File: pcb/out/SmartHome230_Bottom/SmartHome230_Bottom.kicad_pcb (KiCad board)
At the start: 2 copper layers, 130 x 115 mm, 58 parts, among them J1 B2B, J2 12V, J3 Przyciski A, J4 Przyciski B, J5 UART, J6 230V IN, J7 Wyj.1, J8 Wyj.2, K1 SRD-12V, K2 SRD-12V, Q1 BC547, Q2 BC547, SW1 EN, SW2 BOOT, U1 MP1584, U2 AMS1117-3.3, U3 ESP32-WROOM-32

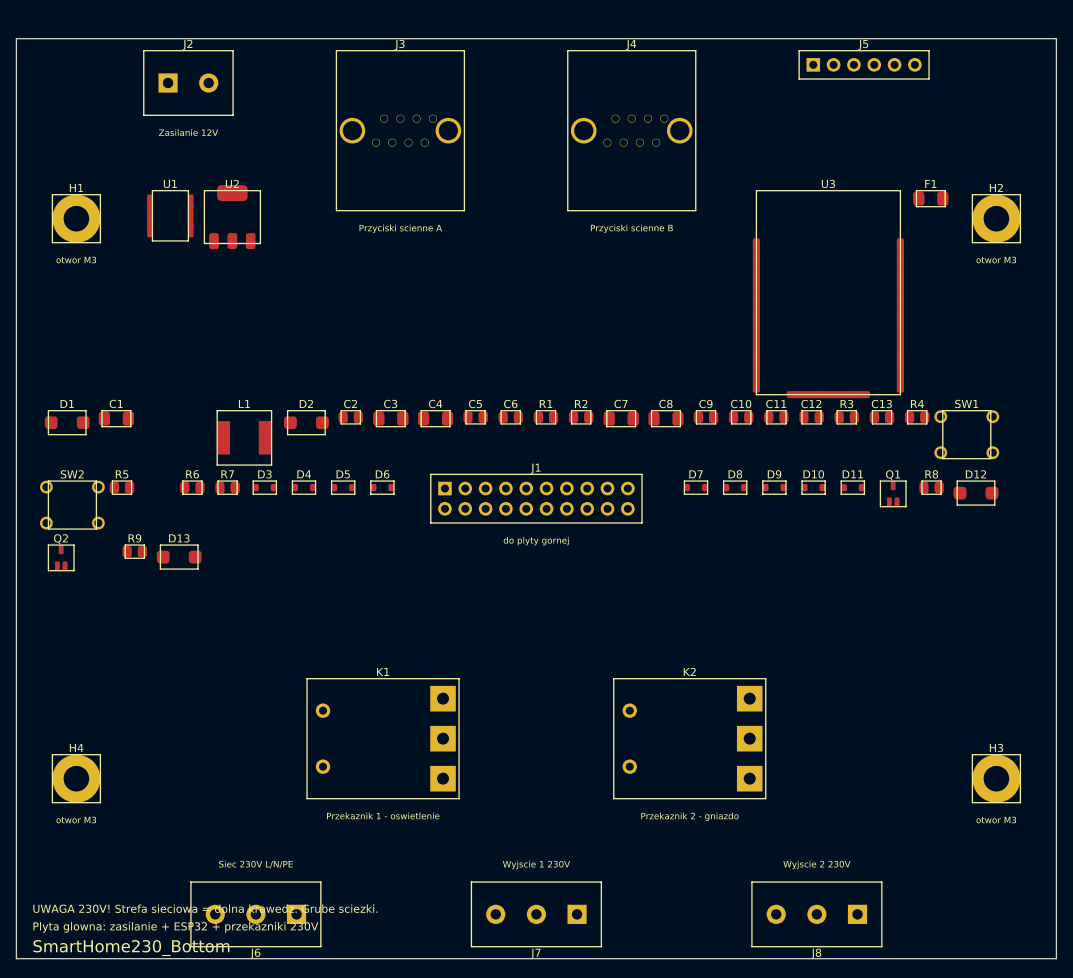
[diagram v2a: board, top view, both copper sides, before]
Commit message: HomeController PRO: sterownik domowy 32 wej / 16 wyj (2 plyty, 24V)
Nowe czesci: ESP32-C3 (modul kastelowany), TJA1051 (CAN), MOV (warystor),
MOSFET mocy DPAK (TO-252). Nowe bloki: wyjscie przekaznikowe 230V, wyjscie
MOSFET DC, bank wejsc RJ45 (TVS/wejscie), RS485, CAN, ESP32-C3, zlacze TFT.

Plyta DOLNA: 24V (bezpiecznik+dioda+MOV+buck5V+LDO3V3), ekspander wyjsc,
8x przekaznik 230V + 8x MOSFET DC, kazde wlasny zacisk; przekazniki we wnetrzu.
Plyta GORNA (wezsza): ESP32-C3 + 2x ekspander (32 wejscia), 8x RJ45, RS485+CAN,
TFT dotykowy. Otwory + B2B wspolne 1:1.

Layout: I/O na krawedzi dla OBU plyt (omija otwory narozne), zaciski 230V na
dolnej krawedzi, przekazniki we wnetrzu. Heurystyka zasilania rozpoznaje V24/Vxx;
regula diod tylko dla zlacz polowych (RJ45/zaciski). Niezawodnosc: TVS na kazdym
I/O, MOV, diody gasnace, pull-down bramek, grube sciezki 230V.

Oba PCB 0/0/0, zwalidowane kiutils (140 i 77 footprintow). Testy 12/12.

Co-Authored-By: Claude Opus 4.8 (1M context) <noreply@anthropic.com>
Claude-Session: https://claude.ai/code/session_01LNGxtK2Jv1rJLBLPTwFQ9C
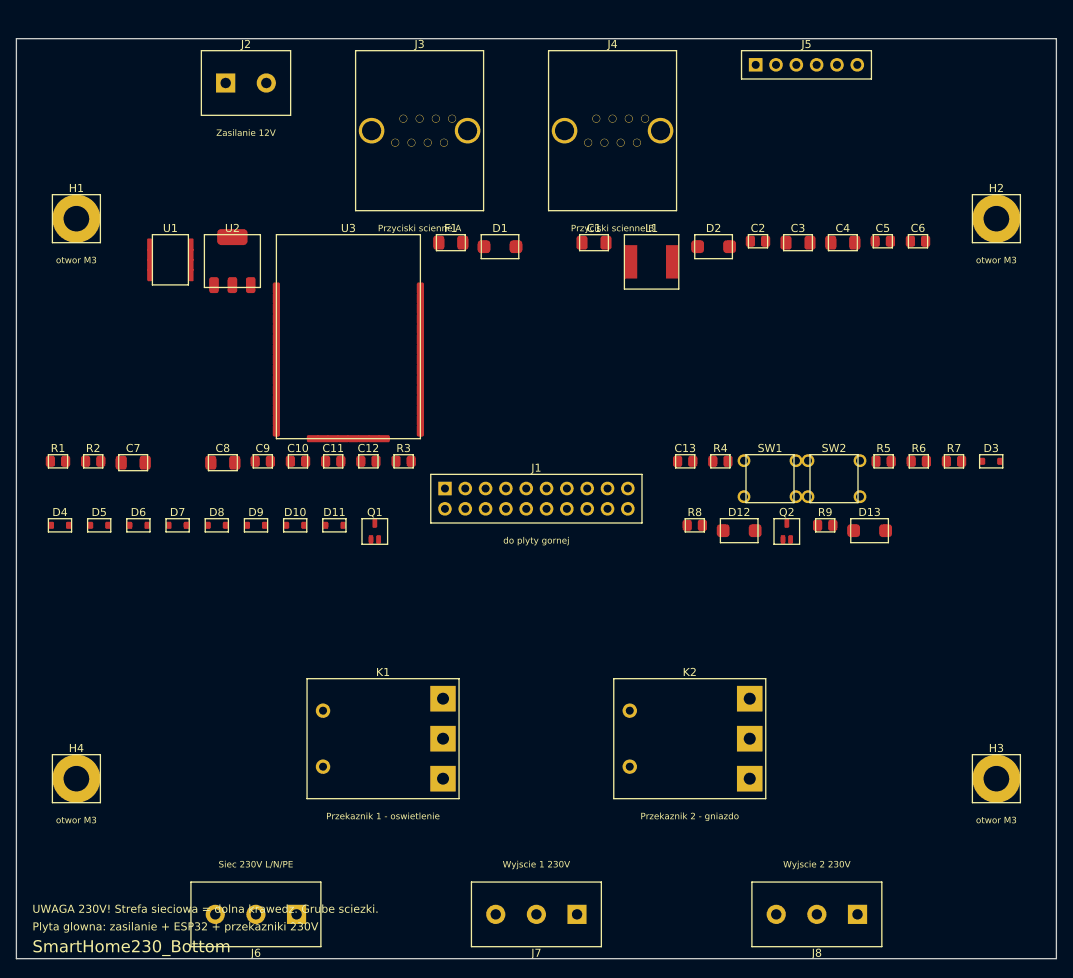
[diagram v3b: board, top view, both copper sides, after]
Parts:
- moved SW2 95.3 mm to (102.2, 55.0)
- moved R5 95.3 mm to (108.4, 52.8)
- moved R7 90.9 mm to (117.2, 52.8)
- moved D3 90.9 mm to (121.8, 52.8)
- moved R6 90.9 mm to (112.8, 52.8)
- moved Q2 90.8 mm to (96.3, 61.6)
- moved D13 86.4 mm to (106.7, 61.5)
- moved R9 86.4 mm to (101.1, 60.8)
- moved D10 65.0 mm to (34.9, 60.8)
- moved D7 65.0 mm to (20.1, 60.8)
- moved D11 65.0 mm to (39.8, 60.8)
- moved D8 65.0 mm to (25.1, 60.8)
- moved D9 65.0 mm to (29.9, 60.8)
- moved Q1 65.0 mm to (44.8, 61.6)
- moved C1 63.6 mm to (72.2, 25.5)
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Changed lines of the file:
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@@
     "pcbforge:ScrewTerminal_1x02_P5.08mm"
     (layer "F.Cu")
-    (at 21.5 5.54)
+    (at 28.7 5.54)
     (descr "Listwa zaciskowa 2x5.08mm")
     (attr through_hole)
@@
     "pcbforge:RJ45_8P8C"
     (layer "F.Cu")
-    (at 48 11.5)
+    (at 50.4 11.5)
     (descr "Gniazdo RJ45 8P8C THT")
     (attr through_hole)
@@
     "pcbforge:RJ45_8P8C"
     (layer "F.Cu")
-    (at 76.92 11.5)
+    (at 74.52 11.5)
     (descr "Gniazdo RJ45 8P8C THT")
     (attr through_hole)
@@
     "pcbforge:F_1206"
     (layer "F.Cu")
-    (at 114.3 20)
+    (at 54.3 25.5)
     (descr "F chip 1206")
     (attr smd)
@@
     "pcbforge:D_SMA"
     (layer "F.Cu")
-    (at 6.35 48)
+    (at 60.45 26)
     (descr "D_SMA")
     (attr smd)
@@
     "pcbforge:CP_1206"
     (layer "F.Cu")
-    (at 12.5 47.5)
+    (at 72.2 25.5)
     (descr "CP chip 1206")
     (attr smd)
@@
     "pcbforge:SOIC-8"
     (layer "F.Cu")
-    (at 19.25 22.14)
+    (at 19.25 27.64)
     (descr "SOIC-8 (1.27mm)")
     (attr smd)
@@
     "pcbforge:L_6x6"
     (layer "F.Cu")
-    (at 28.5 49.9)
+    (at 79.4 27.9)
     (descr "Cewka mocy 6x6mm")
     (attr smd)
@@
     "pcbforge:D_SMA"
     (layer "F.Cu")
-    (at 36.25 48)
+    (at 87.15 26)
     (descr "D_SMA")
     (attr smd)
@@
     "pcbforge:C_0805"
     (layer "F.Cu")
-    (at 41.8 47.33)
+    (at 92.7 25.32)
     (descr "C chip 0805")
     (attr smd)
@@
     "pcbforge:CP_1206"
     (layer "F.Cu")
-    (at 46.8 47.5)
+    (at 97.7 25.5)
     (descr "CP chip 1206")
     (attr smd)
@@
     "pcbforge:CP_1206"
     (layer "F.Cu")
-    (at 52.4 47.5)
+    (at 103.3 25.5)
     (descr "CP chip 1206")
     (attr smd)
@@
     "pcbforge:C_0805"
     (layer "F.Cu")
-    (at 57.4 47.33)
+    (at 108.3 25.32)
     (descr "C chip 0805")
     (attr smd)
@@
     "pcbforge:C_0805"
     (layer "F.Cu")
-    (at 61.8 47.33)
+    (at 112.7 25.32)
     (descr "C chip 0805")
     (attr smd)
@@
     "pcbforge:R_0805"
     (layer "F.Cu")
-    (at 66.2 47.33)
+    (at 5.2 52.83)
     (descr "R chip 0805")
     (attr smd)
@@
     "pcbforge:R_0805"
     (layer "F.Cu")
-    (at 70.6 47.33)
+    (at 9.6 52.83)
     (descr "R chip 0805")
     (attr smd)
@@
     "pcbforge:SOT-223"
     (layer "F.Cu")
-    (at 27 22.3)
+    (at 27 27.8)
     (descr "SOT-223 (regulator LDO)")
     (attr smd)
@@
     "pcbforge:CP_1206"
     (layer "F.Cu")
-    (at 75.6 47.5)
+    (at 14.6 53)
     (descr "CP chip 1206")
     (attr smd)
@@
     "pcbforge:CP_1206"
     (layer "F.Cu")
-    (at 81.2 47.5)
+    (at 25.8 53)
     (descr "CP chip 1206")
     (attr smd)
@@
     "pcbforge:C_0805"
     (layer "F.Cu")
-    (at 86.2 47.33)
+    (at 30.8 52.83)
     (descr "C chip 0805")
     (attr smd)
@@
     "pcbforge:C_0805"
     (layer "F.Cu")
-    (at 90.6 47.33)
+    (at 35.2 52.83)
     (descr "C chip 0805")
     (attr smd)
@@
     "pcbforge:ESP32-WROOM-32"
     (layer "F.Cu")
-    (at 101.5 31.75)
+    (at 41.5 37.25)
     (descr "Modul ESP32-WROOM-32 (38 padow)")
     (attr smd)
@@
     "pcbforge:C_0805"
     (layer "F.Cu")
-    (at 95 47.33)
+    (at 39.6 52.83)
     (descr "C chip 0805")
     (attr smd)
@@
     "pcbforge:C_0805"
     (layer "F.Cu")
-    (at 99.4 47.33)
+    (at 44 52.83)
     (descr "C chip 0805")
     (attr smd)
@@
     "pcbforge:R_0805"
     (layer "F.Cu")
-    (at 103.8 47.33)
+    (at 48.4 52.83)
     (descr "R chip 0805")
     (attr smd)
@@
     "pcbforge:C_0805"
     (layer "F.Cu")
-    (at 108.2 47.33)
+    (at 83.6 52.83)
     (descr "C chip 0805")
     (attr smd)
@@
     "pcbforge:R_0805"
     (layer "F.Cu")
-    (at 112.6 47.33)
+    (at 88 52.83)
     (descr "R chip 0805")
     (attr smd)
@@
     "pcbforge:SW_Push_6mm"
     (layer "F.Cu")
-    (at 118.8 49.5)
+    (at 94.2 55)
     (descr "Tact switch 6mm")
     (attr through_hole)
@@
     "pcbforge:SW_Push_6mm"
     (layer "F.Cu")
-    (at 7 58.3)
+    (at 102.2 55)
     (descr "Tact switch 6mm")
     (attr through_hole)
@@
     "pcbforge:PinHeader_1x06_P2.54mm"
     (layer "F.Cu")
-    (at 105.96 3.27)
+    (at 98.76 3.27)
     (descr "Pin header 1x6")
     (attr through_hole)
@@
     "pcbforge:R_0805"
     (layer "F.Cu")
-    (at 13.2 56.12)
+    (at 108.4 52.83)
     (descr "R chip 0805")
     (attr smd)
@@
     "pcbforge:R_0805"
     (layer "F.Cu")
-    (at 22 56.12)
+    (at 112.8 52.83)
     (descr "R chip 0805")
     (attr smd)
@@
     "pcbforge:R_0805"
     (layer "F.Cu")
-    (at 26.4 56.12)
+    (at 117.2 52.83)
     (descr "R chip 0805")
     (attr smd)
@@
     "pcbforge:D_SOD-323"
     (layer "F.Cu")
-    (at 31.05 56.12)
+    (at 121.85 52.83)
     (descr "D_SOD-323")
     (attr smd)
@@
     "pcbforge:D_SOD-323"
     (layer "F.Cu")
-    (at 35.95 56.12)
+    (at 5.45 60.83)
     (descr "D_SOD-323")
     (attr smd)
@@
     "pcbforge:D_SOD-323"
     (layer "F.Cu")
-    (at 40.85 56.12)
+    (at 10.35 60.83)
     (descr "D_SOD-323")
     (attr smd)
@@
     "pcbforge:D_SOD-323"
     (layer "F.Cu")
-    (at 45.75 56.12)
+    (at 15.25 60.83)
     (descr "D_SOD-323")
     (attr smd)
@@
     "pcbforge:D_SOD-323"
     (layer "F.Cu")
-    (at 84.95 56.12)
+    (at 20.15 60.83)
     (descr "D_SOD-323")
     (attr smd)
@@
     "pcbforge:D_SOD-323"
     (layer "F.Cu")
-    (at 89.85 56.12)
+    (at 25.05 60.83)
     (descr "D_SOD-323")
     (attr smd)
@@
     "pcbforge:D_SOD-323"
     (layer "F.Cu")
-    (at 94.75 56.12)
+    (at 29.95 60.83)
     (descr "D_SOD-323")
     (attr smd)
@@
     "pcbforge:D_SOD-323"
     (layer "F.Cu")
-    (at 99.65 56.12)
+    (at 34.85 60.83)
     (descr "D_SOD-323")
     (attr smd)
@@
     "pcbforge:D_SOD-323"
     (layer "F.Cu")
-    (at 104.55 56.12)
+    (at 39.75 60.83)
     (descr "D_SOD-323")
     (attr smd)
@@
     "pcbforge:SOT-23-3"
     (layer "F.Cu")
-    (at 109.6 56.9)
+    (at 44.8 61.6)
     (descr "SOT-23-3")
     (attr smd)
@@
     "pcbforge:R_0805"
     (layer "F.Cu")
-    (at 114.4 56.12)
+    (at 84.8 60.83)
     (descr "R chip 0805")
     (attr smd)
@@
     "pcbforge:D_SMA"
     (layer "F.Cu")
-    (at 119.95 56.8)
+    (at 90.35 61.5)
     (descr "D_SMA")
     (attr smd)
@@
     "pcbforge:SOT-23-3"
     (layer "F.Cu")
-    (at 5.6 64.9)
+    (at 96.3 61.6)
     (descr "SOT-23-3")
     (attr smd)
@@
     "pcbforge:R_0805"
     (layer "F.Cu")
-    (at 14.8 64.12)
+    (at 101.1 60.83)
     (descr "R chip 0805")
     (attr smd)
@@
     "pcbforge:D_SMA"
     (layer "F.Cu")
-    (at 20.35 64.8)
+    (at 106.65 61.5)
     (descr "D_SMA")
     (attr smd)

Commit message: ESP32-S3 + przyciski TFT; kompaktowy layout (szerokosc z liczby zlacz, 2 rzedy)
- Przejscie ESP32-C3 -> ESP32-S3 (duzo GPIO): niezalezne RS485/CAN, dotyk z IRQ,
  4 przyciski nawigacji TFT (GORA/DOL/OK/WSTECZ). Nowa czesc ESP32-S3-WROOM-1.
- Layout: I/O wzdluz krawedzi w 2 rzedach (podwojne w pionie), szerokosc plytki
  wynika z LICZBY zlacz (zmienne szerokosci kolumn) - wejscia na gornej krawedzi,
  wyjscia (zaciski) na dolnej. auto_frame() dobiera ciasna wspolna ramke.
- Przekazniki pakowane w strefe 230V (kilka rzedow) omijajaca otwory.
- HomeCtrlPro: 280x185 -> 168x192 mm, mniej pustego miejsca. Oba 0/0/0.

Testy 12/12, zwalidowane kiutils. Bloki: esp32s3, button.

Co-Authored-By: Claude Opus 4.8 (1M context) <noreply@anthropic.com>
Claude-Session: https://claude.ai/code/session_01LNGxtK2Jv1rJLBLPTwFQ9C
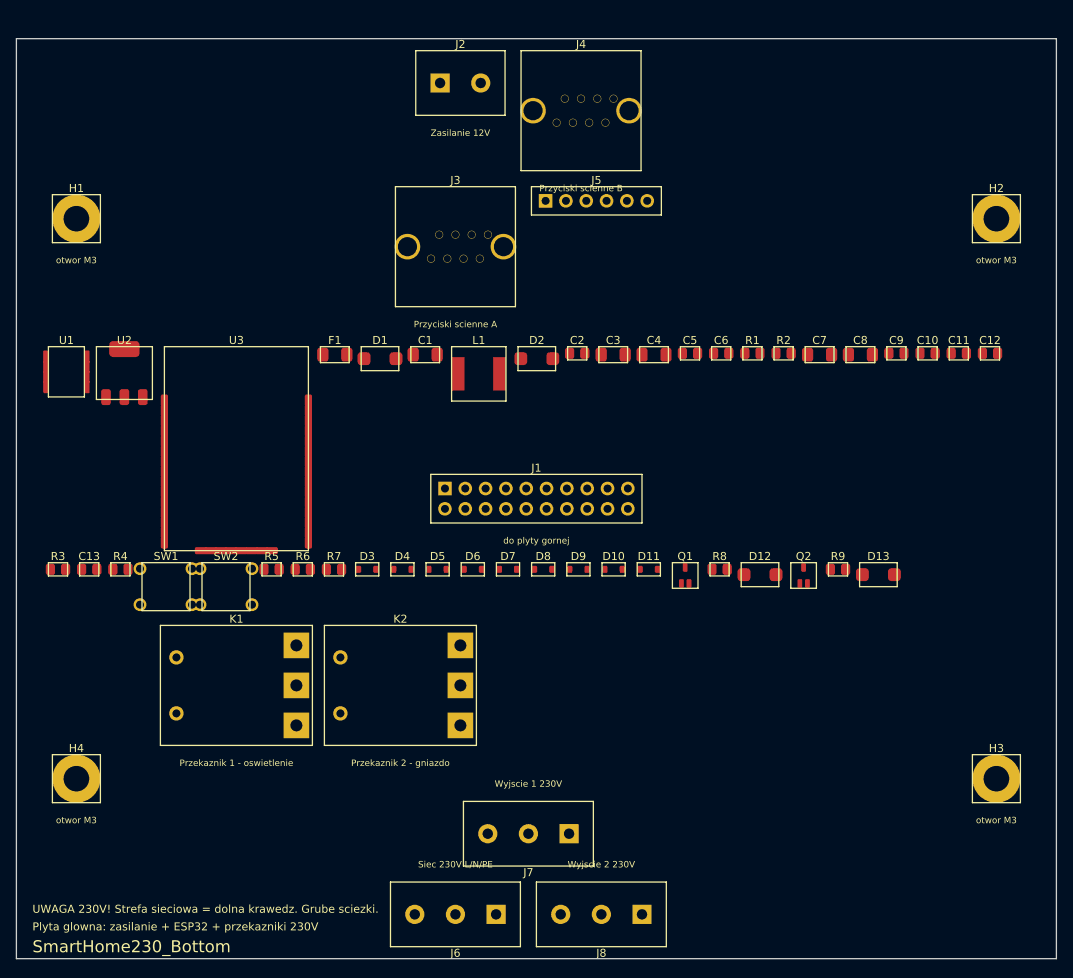
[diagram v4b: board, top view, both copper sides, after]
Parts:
- moved R1 87.8 mm to (92.0, 39.3)
- moved R2 87.3 mm to (95.9, 39.3)
- moved C7 86.9 mm to (100.4, 39.5)
- moved C8 80.8 mm to (105.5, 39.5)
- moved C9 80.3 mm to (110.0, 39.3)
- moved C10 79.8 mm to (113.9, 39.3)
- moved C11 79.4 mm to (117.8, 39.3)
- moved D3 79.2 mm to (43.9, 66.3)
- moved C12 78.9 mm to (121.7, 39.3)
- moved R7 78.7 mm to (39.7, 66.3)
- moved R6 78.2 mm to (35.8, 66.3)
- moved R5 77.7 mm to (31.9, 66.3)
- moved SW2 77.2 mm to (26.2, 68.5)
- moved SW1 76.7 mm to (18.7, 68.5)
- moved R4 76.2 mm to (13.0, 66.3)
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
